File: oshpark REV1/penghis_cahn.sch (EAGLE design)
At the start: 67 parts, among them IC1 PCF8574T, P0 TPB1,27, P1 TPB1,27, T1 BC847, T2 BC847, U1 MCP73831

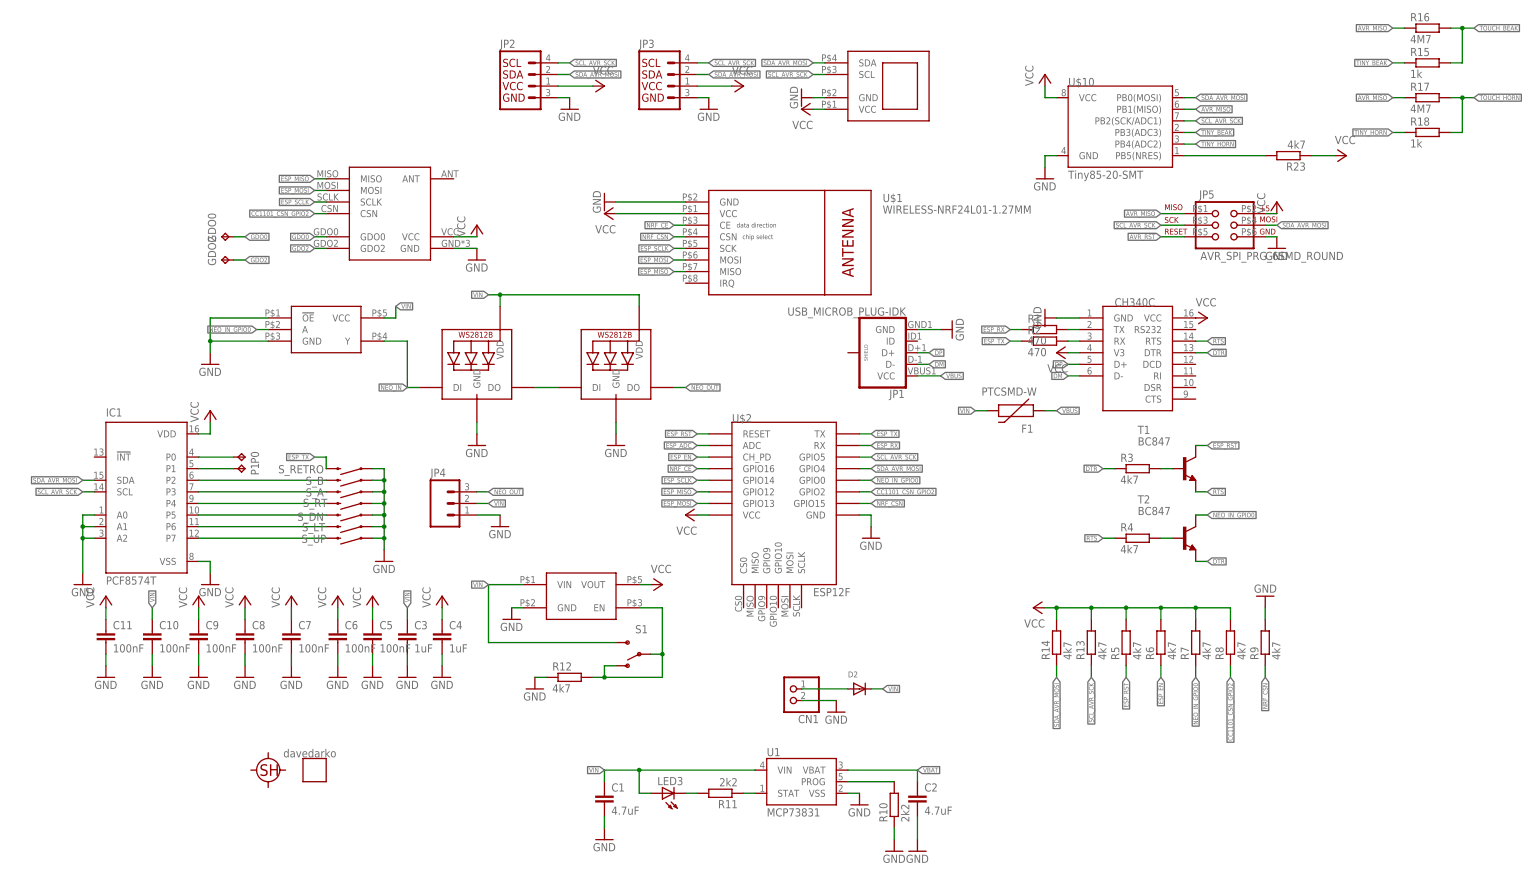
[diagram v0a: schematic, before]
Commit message: minor updates
added TPS22918 for neopixels
updated labels
moved in nrf24 module
added SAO V1.69bis
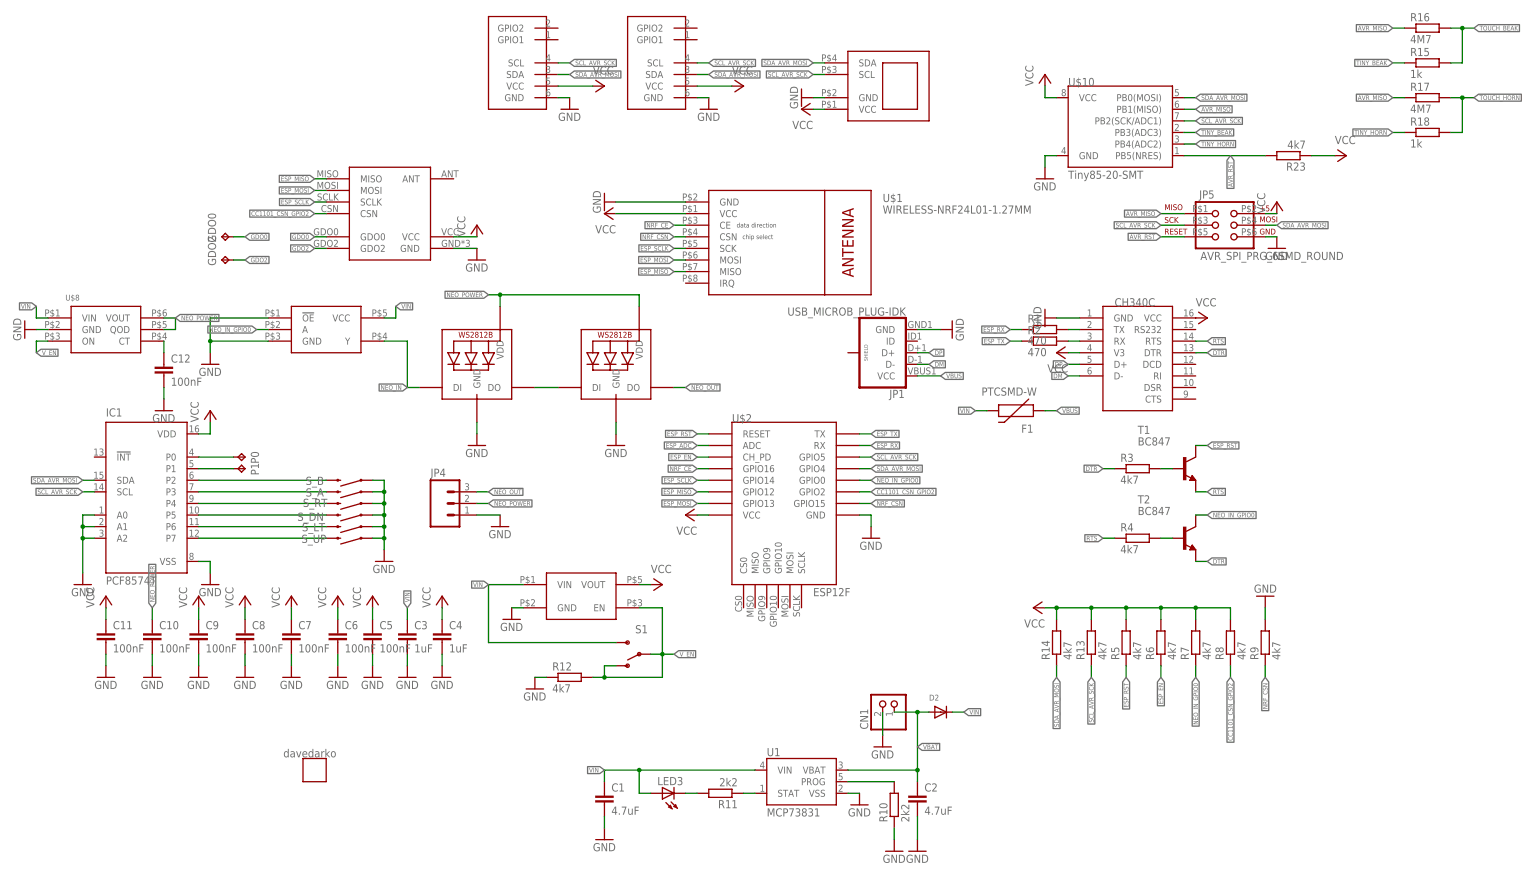
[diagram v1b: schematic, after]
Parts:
- removed JP2, JP3: (no value), SparkFun-Connectors:I2C_STANDARDI2C_SAO
- removed S_RETRO: SWITCH-MOMENTARY-2-SMD-1101NE, SparkFun-Electromechanical:SWITCH-MOMENTARY-2-SMD-1101NE
- added C12: 100nF, rcl:C-EUC0805
- added SAO1, SAO2: SAO-SHITTY-ADDONMASTER, SparkFun-Connectors:SAO-SHITTY-ADDONMASTER
- U$8: value OSHPARK_100MIL_TXT -> TPS22917; device LOGOS:OSHPARK_100MIL_TXT -> tps22917:TPS22917
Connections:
- removed net N$9: R12.2, S1.O, S1.P, U$3.EN
- new net N$16: C12.1, U$8.CT
- new net NEO_POWER: C10.1, JP4.2, LED1.VDD, LED2.VDD, U$8.QOD, U$8.VOUT
- new net V_EN: R12.2, S1.O, S1.P, U$3.EN, U$8.ON
- net ESP_TX: no longer S_RETRO.2
- net GND: now also C12.2, SAO1.GND, SAO2.GND, U$8.GND; no longer JP2.GND, JP3.GND, S_RETRO.1
- net SCL_AVR_SCK: now also SAO1.SCL, SAO2.SCL; no longer JP2.SCL, JP3.SCL
- net SDA_AVR_MOSI: now also SAO1.SDA, SAO2.SDA; no longer JP2.SDA, JP3.SDA
- net VCC: now also SAO1.VCC, SAO2.VCC; no longer JP2.VCC, JP3.VCC
- net VIN: now also U$8.VIN; no longer C10.1, JP4.2, LED1.VDD, LED2.VDD
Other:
- moved on the sheet: CN1, D2
